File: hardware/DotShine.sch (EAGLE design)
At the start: 62 parts, among them CN1 1X4-BIG, IC1 CAT24M010TS, IC3 SI1145, J3 USB-MICROB, U1 ATMEGA328P-MU-QFN32, U2 TMP102, U3 ATSHA204-TSU, U4 JDY-16, X2 MC-RTC-RV-4162-C7-I2C, X3 S4B-ZR

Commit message: Initial bluetooth integration
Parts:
- removed X3: S4B-ZR, con-jst:S4B-ZR
- added U$4: JST-8, mihai_connectors_jst:JST-8
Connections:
- removed net N$4: LED1.CRED, R1C.2
- new net RXD_IN: LED1.CRED, R1C.2, U$4.8
- net +3V3: now also U$4.5
- net +5V: now also U$4.1; no longer X3-4.1
- net GND: now also U$4.4; no longer X3-1.1
- net OUTAB: now also U$4.2; no longer X3-3.1
- net SCL: now also U$4.6
- net SDA: now also U$4.7
- net TXD_OUT: now also U$4.3; no longer X3-2.1
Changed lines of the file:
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@@
 <?xml version="1.0" encoding="utf-8"?>
 <!DOCTYPE eagle SYSTEM "eagle.dtd">
-<eagle version="7.7.0">
+<eagle version="9.1.0">
 <drawing>
 <settings>
 <setting alwaysvectorfont="no"/>
+<setting keepoldvectorfont="yes"/>
 <setting verticaltext="up"/>
 </settings>
-<grid distance="0.1" unitdist="inch" unit="inch" style="lines" multiple="1" display="no" altdistance="0.01" altunitdist="inch" altunit="inch"/>
+<grid distance="0.05" unitdist="inch" unit="inch" style="lines" multiple="1" display="no" altdistance="0.01" altunitdist="inch" altunit="inch"/>
 <layers>
 <layer number="1" name="Top" color="4" fill="1" visible="no" active="no"/>
@@
 <layer number="59" name="tCarbon" color="7" fill="1" visible="no" active="no"/>
 <layer number="60" name="bCarbon" color="7" fill="1" visible="no" active="no"/>
+<layer number="88" name="SimResults" color="9" fill="1" visible="yes" active="yes"/>
+<layer number="89" name="SimProbes" color="9" fill="1" visible="yes" active="yes"/>
 <layer number="90" name="Modules" color="5" fill="1" visible="yes" active="yes"/>
 <layer number="91" name="Nets" color="2" fill="1" visible="yes" active="yes"/>
@@
 <part name="+3V6" library="supply1" deviceset="+3V3" device=""/>
 <part name="SUPPLY2" library="supply2" deviceset="GND" device=""/>
-<part name="SUPPLY7" library="supply2" deviceset="GND" device=""/>
-<part name="X3" library="con-jst" deviceset="?4B-ZR" device="S"/>
-<part name="P+2" library="supply1" deviceset="+5V" device=""/>
 <part name="LED2" library="SparkFun" deviceset="LED" device="0603"/>
 <part name="LED3" library="SparkFun" deviceset="LED" device="0603"/>
@@
 <part name="SUPPLY9" library="supply2" deviceset="GND" device=""/>
 <part name="+3V22" library="supply1" deviceset="+3V3" device=""/>
+<part name="U$4" library="mihai_connectors_jst" deviceset="JST-8" device=""/>
+<part name="SUPPLY12" library="supply2" deviceset="GND" device=""/>
+<part name="P+1" library="supply1" deviceset="+5V" device=""/>
+<part name="+3V23" library="supply1" deviceset="+3V3" device=""/>
 </parts>
 <sheets>
@@
 <instance part="+3V6" gate="G$1" x="43.18" y="115.57" rot="R90"/>
 <instance part="SUPPLY2" gate="GND" x="52.07" y="110.49"/>
-<instance part="SUPPLY7" gate="GND" x="97.79" y="125.73" rot="R270"/>
-<instance part="X3" gate="-1" x="111.76" y="125.73"/>
-<instance part="X3" gate="-2" x="111.76" y="123.19"/>
-<instance part="X3" gate="-3" x="111.76" y="120.65"/>
-<instance part="X3" gate="-4" x="111.76" y="118.11"/>
-<instance part="P+2" gate="1" x="83.82" y="118.11" rot="R90"/>
 <instance part="LED2" gate="G$1" x="137.16" y="142.24" rot="R90"/>
 <instance part="LED3" gate="G$1" x="139.7" y="132.08" rot="R270"/>
@@
 <instance part="SUPPLY9" gate="GND" x="137.16" y="-330.2" rot="MR270"/>
 <instance part="+3V22" gate="G$1" x="76.2" y="-317.5"/>
+<instance part="U$4" gate="G$1" x="134.62" y="-412.75"/>
+<instance part="SUPPLY12" gate="GND" x="113.03" y="-397.51" rot="R270"/>
+<instance part="P+1" gate="1" x="116.84" y="-389.89" rot="R90"/>
+<instance part="+3V23" gate="G$1" x="111.76" y="-400.05" rot="R90"/>
 </instances>
 <busses>
@@
 <pinref part="R4" gate="D" pin="2"/>
 <pinref part="SUPPLY29" gate="GND" pin="GND"/>
-</segment>
-<segment>
-<pinref part="X3" gate="-1" pin="1"/>
-<pinref part="SUPPLY7" gate="GND" pin="GND"/>
-<wire x1="106.68" y1="125.73" x2="100.33" y2="125.73" width="0.1524" layer="91"/>
 </segment>
 <segment>
@@
 <junction x="134.62" y="-330.2"/>
 </segment>
+<segment>
+<pinref part="SUPPLY12" gate="GND" pin="GND"/>
+<wire x1="129.54" y1="-397.51" x2="115.57" y2="-397.51" width="0.1524" layer="91"/>
+<pinref part="U$4" gate="G$1" pin="4"/>
+</segment>
 </net>
 <net name="SDA" class="0">
@@
 <wire x1="124.46" y1="-342.9" x2="134.62" y2="-342.9" width="0.1524" layer="91"/>
 <label x="134.62" y="-342.9" size="1.27" layer="95" xref="yes"/>
+</segment>
+<segment>
+<pinref part="U$4" gate="G$1" pin="7"/>
+<wire x1="129.54" y1="-405.13" x2="125.73" y2="-405.13" width="0.1524" layer="91"/>
+<label x="125.73" y="-405.13" size="1.27" layer="95" rot="R180" xref="yes"/>
 </segment>
 </net>
@@
 <wire x1="76.2" y1="-320.04" x2="76.2" y2="-330.2" width="0.1524" layer="91"/>
 </segment>
+<segment>
+<pinref part="U$4" gate="G$1" pin="5"/>
+<pinref part="+3V23" gate="G$1" pin="+3V3"/>
+<wire x1="129.54" y1="-400.05" x2="114.3" y2="-400.05" width="0.1524" layer="91"/>
+</segment>
 </net>
 <net name="ADCENA" class="0">
@@
 <label x="134.62" y="-340.36" size="1.27" layer="95" xref="yes"/>
 </segment>
+<segment>
+<pinref part="U$4" gate="G$1" pin="6"/>
+<wire x1="129.54" y1="-402.59" x2="125.73" y2="-402.59" width="0.1524" layer="91"/>
+<label x="125.73" y="-402.59" size="1.27" layer="95" rot="R180" xref="yes"/>
+</segment>
 </net>
 <net name="PUSH" class="0">
@@
 </segment>
 <segment>
-<pinref part="X3" gate="-2" pin="1"/>
-<wire x1="106.68" y1="123.19" x2="86.36" y2="123.19" width="0.1524" layer="91"/>
-<label x="86.36" y="123.19" size="1.27" layer="95" rot="R180" xref="yes"/>
+<wire x1="129.54" y1="-394.97" x2="110.49" y2="-394.97" width="0.1524" layer="91"/>
+<label x="110.49" y="-394.97" size="1.27" layer="95" rot="R180" xref="yes"/>
+<pinref part="U$4" gate="G$1" pin="3"/>
 </segment>
 </net>
@@
 </segment>
 </net>
-<net name="N$4" class="0">
-<segment>
-<pinref part="LED1" gate="G$1" pin="CRED"/>
-<wire x1="-27.94" y1="68.58" x2="-33.02" y2="68.58" width="0.1524" layer="91"/>
-<wire x1="-33.02" y1="68.58" x2="-33.02" y2="66.04" width="0.1524" layer="91"/>
-<pinref part="R1" gate="C" pin="2"/>
-</segment>
-</net>
 <net name="+5V" class="0">
-<segment>
-<pinref part="X3" gate="-4" pin="1"/>
-<pinref part="P+2" gate="1" pin="+5V"/>
-<wire x1="106.68" y1="118.11" x2="86.36" y2="118.11" width="0.1524" layer="91"/>
-</segment>
 <segment>
 <pinref part="P+4" gate="1" pin="+5V"/>
@@
 <pinref part="P+3" gate="1" pin="+5V"/>
 <wire x1="67.31" y1="-48.26" x2="53.34" y2="-48.26" width="0.1524" layer="91"/>
+</segment>
+<segment>
+<pinref part="P+1" gate="1" pin="+5V"/>
+<wire x1="129.54" y1="-389.89" x2="119.38" y2="-389.89" width="0.1524" layer="91"/>
+<pinref part="U$4" gate="G$1" pin="1"/>
 </segment>
 </net>
@@
 <net name="OUTAB" class="0">
 <segment>
-<pinref part="X3" gate="-3" pin="1"/>
-<wire x1="106.68" y1="120.65" x2="86.36" y2="120.65" width="0.1524" layer="91"/>
-<label x="86.36" y="120.65" size="1.27" layer="95" rot="R180" xref="yes"/>
 <pinref part="R4" gate="A" pin="2"/>
-<wire x1="106.68" y1="120.65" x2="118.11" y2="120.65" width="0.1524" layer="91"/>
-<wire x1="118.11" y1="120.65" x2="118.11" y2="132.08" width="0.1524" layer="91"/>
-<junction x="106.68" y="120.65"/>
+<wire x1="113.03" y1="132.08" x2="118.11" y2="132.08" width="0.1524" layer="91"/>
+<label x="113.03" y="132.08" size="1.27" layer="95" rot="R180" xref="yes"/>
 </segment>
 <segment>
@@
 <wire x1="76.2" y1="83.82" x2="78.74" y2="83.82" width="0.1524" layer="91"/>
 <label x="78.74" y="83.82" size="1.27" layer="95" xref="yes"/>
+</segment>
+<segment>
+<wire x1="129.54" y1="-392.43" x2="110.49" y2="-392.43" width="0.1524" layer="91"/>
+<label x="110.49" y="-392.43" size="1.27" layer="95" rot="R180" xref="yes"/>
+<pinref part="U$4" gate="G$1" pin="2"/>
 </segment>
 </net>
@@
 <pinref part="U4" gate="G$1" pin="ALED"/>
 <wire x1="124.46" y1="-347.98" x2="134.62" y2="-347.98" width="0.1524" layer="91"/>
+<label x="134.62" y="-347.98" size="1.27" layer="95" xref="yes"/>
+</segment>
+</net>
+<net name="RXD_IN" class="0">
+<segment>
+<pinref part="U$4" gate="G$1" pin="8"/>
+<wire x1="129.54" y1="-407.67" x2="125.73" y2="-407.67" width="0.1524" layer="91"/>
+<label x="125.73" y="-407.67" size="1.27" layer="95" rot="R180" xref="yes"/>
+</segment>
+<segment>
+<pinref part="LED1" gate="G$1" pin="CRED"/>
+<wire x1="-27.94" y1="68.58" x2="-33.02" y2="68.58" width="0.1524" layer="91"/>
+<wire x1="-33.02" y1="68.58" x2="-33.02" y2="66.04" width="0.1524" layer="91"/>
+<pinref part="R1" gate="C" pin="2"/>
+<wire x1="-27.94" y1="68.58" x2="-27.94" y2="38.1" width="0.1524" layer="91"/>
+<junction x="-27.94" y="68.58"/>
+<label x="-27.94" y="38.1" size="1.27" layer="95" rot="R270" xref="yes"/>
 </segment>
 </net>
@@
 which will not be processed correctly with this version.
 </note>
+<note version="8.3" severity="warning">
+Since Version 8.3, EAGLE supports URNs for individual library
+assets (packages, symbols, and devices). The URNs of those assets
+will not be understood (or retained) with this version.
+</note>
 </compatibility>

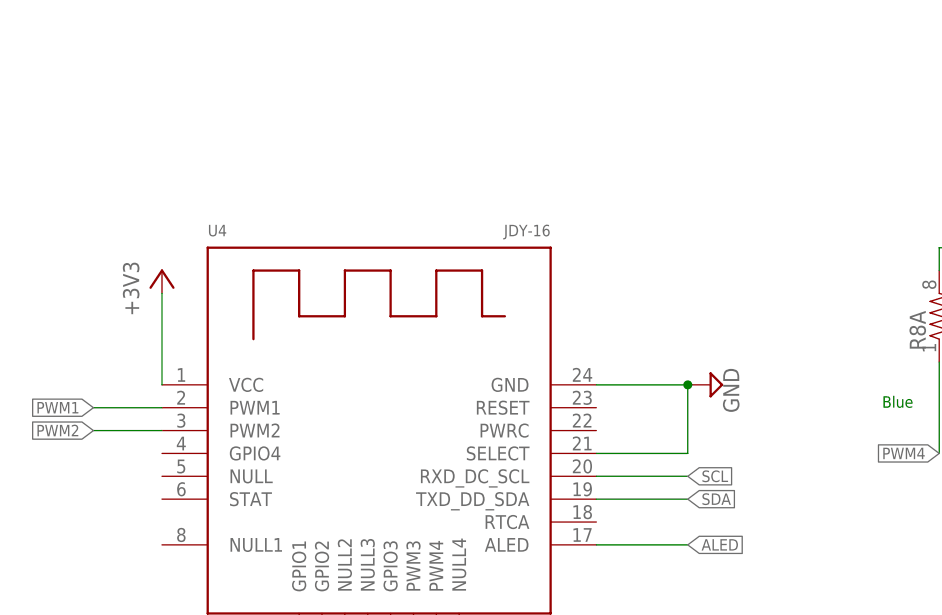
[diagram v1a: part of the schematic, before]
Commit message: Add PWRC connection for BT, needed to assert low to reenable I2C
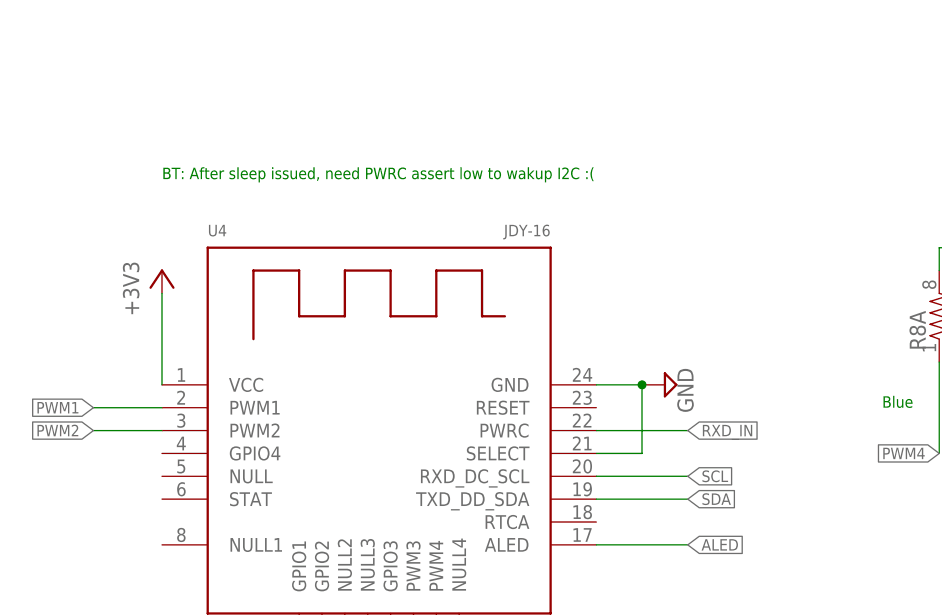
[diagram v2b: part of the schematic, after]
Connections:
- net RXD_IN: now also U4.PWRC
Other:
- note added: "BT: After sleep issued, need PWRC assert low to wakup I2C :("
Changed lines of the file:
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@@
 <setting verticaltext="up"/>
 </settings>
-<grid distance="0.05" unitdist="inch" unit="inch" style="lines" multiple="1" display="no" altdistance="0.01" altunitdist="inch" altunit="inch"/>
+<grid distance="0.1" unitdist="inch" unit="inch" style="lines" multiple="1" display="no" altdistance="0.01" altunitdist="inch" altunit="inch"/>
 <layers>
 <layer number="1" name="Top" color="4" fill="1" visible="no" active="no"/>
@@
 <text x="184.658" y="-332.74" size="1.27" layer="91">Red</text>
 <text x="156.21" y="-332.74" size="1.27" layer="91">Blue</text>
+<text x="76.2" y="-307.34" size="1.27" layer="91">BT: After sleep issued, need PWRC assert low to wakup I2C :(</text>
 </plain>
 <instances>
@@
 <instance part="R8" gate="C" x="238.76" y="-309.88" rot="R270"/>
 <instance part="R8" gate="D" x="182.88" y="-322.58" rot="R90"/>
-<instance part="SUPPLY9" gate="GND" x="137.16" y="-330.2" rot="MR270"/>
+<instance part="SUPPLY9" gate="GND" x="132.08" y="-330.2" rot="MR270"/>
 <instance part="+3V22" gate="G$1" x="76.2" y="-317.5"/>
 <instance part="U$4" gate="G$1" x="134.62" y="-412.75"/>
@@
 <pinref part="SUPPLY9" gate="GND" pin="GND"/>
 <pinref part="U4" gate="G$1" pin="GND"/>
-<wire x1="134.62" y1="-330.2" x2="124.46" y2="-330.2" width="0.1524" layer="91"/>
+<wire x1="129.54" y1="-330.2" x2="124.46" y2="-330.2" width="0.1524" layer="91"/>
 <pinref part="U4" gate="G$1" pin="SELECT"/>
-<wire x1="124.46" y1="-337.82" x2="134.62" y2="-337.82" width="0.1524" layer="91"/>
-<wire x1="134.62" y1="-337.82" x2="134.62" y2="-330.2" width="0.1524" layer="91"/>
-<junction x="134.62" y="-330.2"/>
+<wire x1="124.46" y1="-337.82" x2="129.54" y2="-337.82" width="0.1524" layer="91"/>
+<wire x1="129.54" y1="-337.82" x2="129.54" y2="-330.2" width="0.1524" layer="91"/>
+<junction x="129.54" y="-330.2"/>
 </segment>
 <segment>
@@
 <label x="-27.94" y="38.1" size="1.27" layer="95" rot="R270" xref="yes"/>
 </segment>
-</net>
+<segment>
+<pinref part="U4" gate="G$1" pin="PWRC"/>
+<wire x1="124.46" y1="-335.28" x2="134.62" y2="-335.28" width="0.1524" layer="91"/>
+<label x="134.62" y="-335.28" size="1.27" layer="95" xref="yes"/>
+</segment>
+</net>

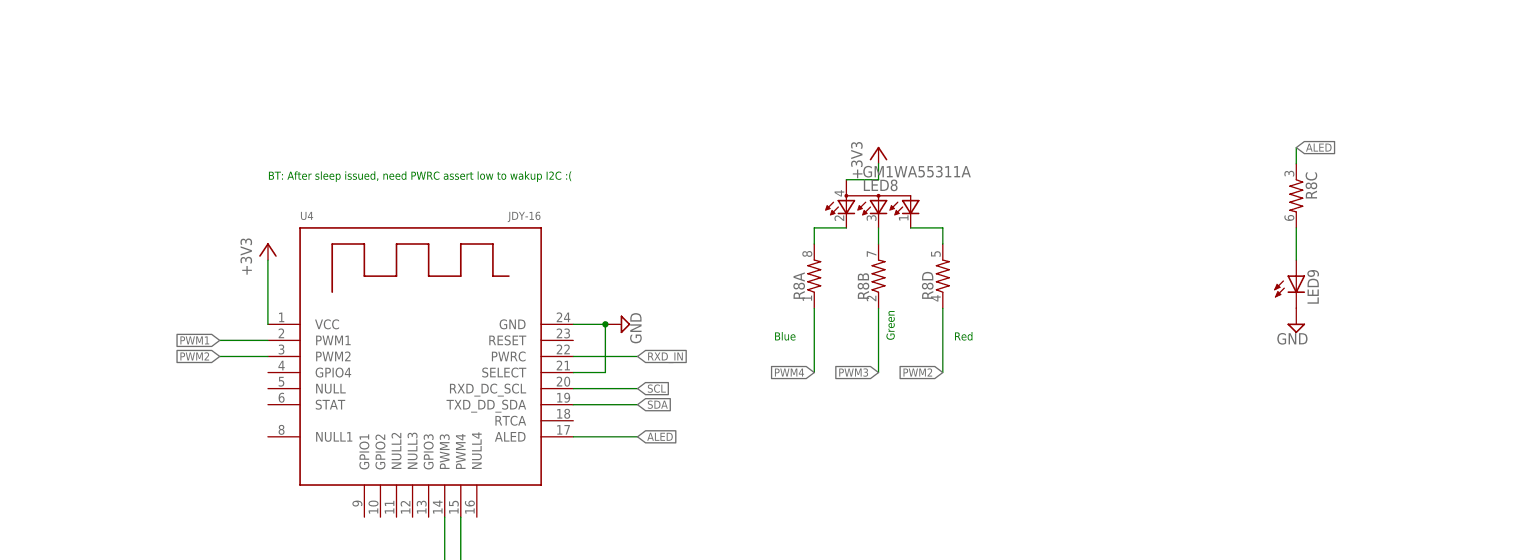
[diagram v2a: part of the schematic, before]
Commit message: Connect BT Stat to INT_MULTIPLE, SJ on ALED
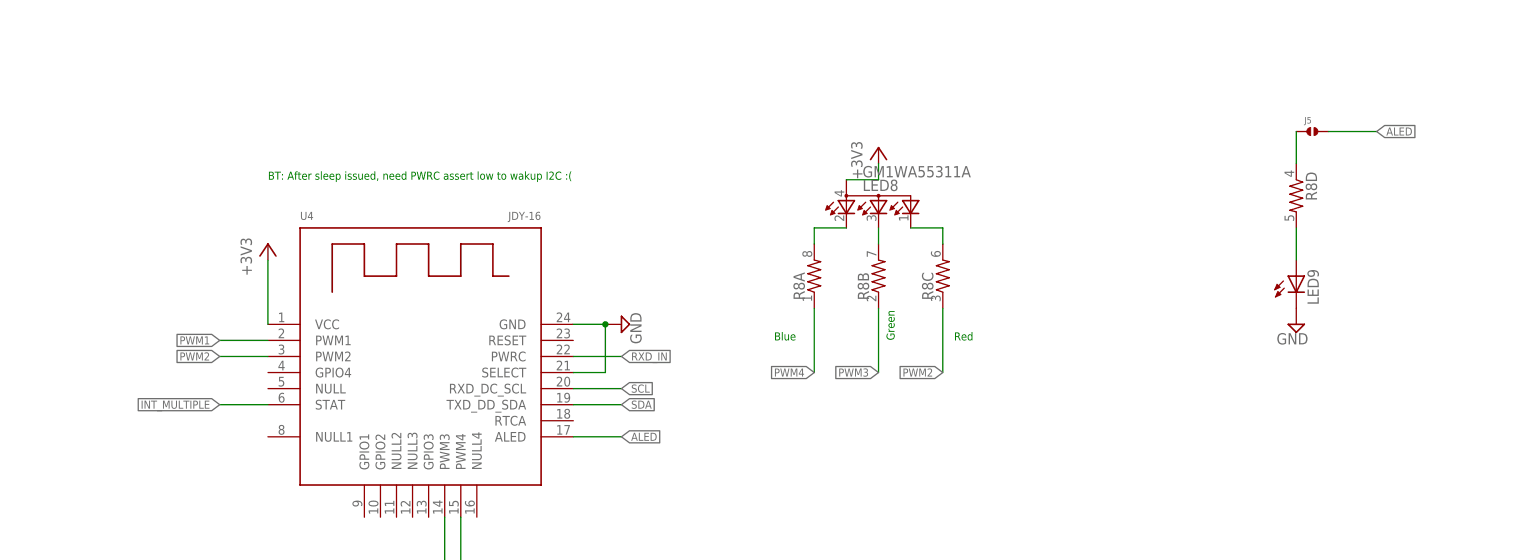
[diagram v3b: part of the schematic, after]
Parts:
- added J5: (no value), solderjumper:SOLDERJUMPER.2.MED
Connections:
- removed net BT_RED: LED8.CGREEN, R8D.2
- removed net N$34: LED9.A, R8C.2
- new net N$1: LED8.CGREEN, R8C.2
- new net N$2: J5.1, R8D.1
- new net N$4: LED9.A, R8D.2
- net ALED: now also J5.2; no longer R8C.1
- net INT_MULTIPLE: now also U4.STAT
- net PWM2: now also R8C.1; no longer R8D.1
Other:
- moved on the sheet: R8C, R8D
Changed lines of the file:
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@@
 <part name="P+1" library="supply1" deviceset="+5V" device=""/>
 <part name="+3V23" library="supply1" deviceset="+3V3" device=""/>
+<part name="J5" library="solderjumper" deviceset="SOLDERJUMPER.2" device=".MED"/>
 </parts>
 <sheets>
@@
 <instance part="R8" gate="A" x="162.56" y="-322.58" rot="R90"/>
 <instance part="R8" gate="B" x="172.72" y="-322.58" rot="R90"/>
-<instance part="R8" gate="C" x="238.76" y="-309.88" rot="R270"/>
-<instance part="R8" gate="D" x="182.88" y="-322.58" rot="R90"/>
+<instance part="R8" gate="C" x="182.88" y="-322.58" rot="R90"/>
+<instance part="R8" gate="D" x="238.76" y="-309.88" rot="R270"/>
 <instance part="SUPPLY9" gate="GND" x="132.08" y="-330.2" rot="MR270"/>
 <instance part="+3V22" gate="G$1" x="76.2" y="-317.5"/>
@@
 <instance part="P+1" gate="1" x="116.84" y="-389.89" rot="R90"/>
 <instance part="+3V23" gate="G$1" x="111.76" y="-400.05" rot="R90"/>
+<instance part="J5" gate="G$1" x="241.3" y="-299.72"/>
 </instances>
 <busses>
@@
 <segment>
 <pinref part="U4" gate="G$1" pin="TXD_DD_SDA"/>
-<wire x1="124.46" y1="-342.9" x2="134.62" y2="-342.9" width="0.1524" layer="91"/>
-<label x="134.62" y="-342.9" size="1.27" layer="95" xref="yes"/>
+<wire x1="124.46" y1="-342.9" x2="132.08" y2="-342.9" width="0.1524" layer="91"/>
+<label x="132.08" y="-342.9" size="1.27" layer="95" xref="yes"/>
 </segment>
 <segment>
@@
 <segment>
 <pinref part="U4" gate="G$1" pin="RXD_DC_SCL"/>
-<wire x1="124.46" y1="-340.36" x2="134.62" y2="-340.36" width="0.1524" layer="91"/>
-<label x="134.62" y="-340.36" size="1.27" layer="95" xref="yes"/>
+<wire x1="124.46" y1="-340.36" x2="132.08" y2="-340.36" width="0.1524" layer="91"/>
+<label x="132.08" y="-340.36" size="1.27" layer="95" xref="yes"/>
 </segment>
 <segment>
@@
 <label x="78.74" y="60.96" size="1.27" layer="95" xref="yes"/>
 </segment>
+<segment>
+<pinref part="U4" gate="G$1" pin="STAT"/>
+<wire x1="76.2" y1="-342.9" x2="68.58" y2="-342.9" width="0.1524" layer="91"/>
+<label x="68.58" y="-342.9" size="1.27" layer="95" rot="R180" xref="yes"/>
+</segment>
 </net>
 <net name="OUTAB" class="0">
@@
 </segment>
 </net>
-<net name="BT_RED" class="0">
-<segment>
-<pinref part="R8" gate="D" pin="2"/>
-<pinref part="LED8" gate="G$1" pin="CGREEN"/>
-<wire x1="182.88" y1="-317.5" x2="182.88" y2="-314.96" width="0.1524" layer="91"/>
-<wire x1="182.88" y1="-314.96" x2="177.8" y2="-314.96" width="0.1524" layer="91"/>
-</segment>
-</net>
-<net name="N$34" class="0">
-<segment>
-<pinref part="R8" gate="C" pin="2"/>
-<pinref part="LED9" gate="G$1" pin="A"/>
-<wire x1="238.76" y1="-314.96" x2="238.76" y2="-320.04" width="0.1524" layer="91"/>
-</segment>
-</net>
 <net name="BT_GREEN" class="0">
 <segment>
@@
 </segment>
 <segment>
-<pinref part="R8" gate="D" pin="1"/>
+<pinref part="R8" gate="C" pin="1"/>
 <wire x1="182.88" y1="-327.66" x2="182.88" y2="-337.82" width="0.1524" layer="91"/>
 <label x="182.88" y="-337.82" size="1.27" layer="95" rot="R180" xref="yes"/>
@@
 <net name="ALED" class="0">
 <segment>
-<pinref part="R8" gate="C" pin="1"/>
-<wire x1="238.76" y1="-304.8" x2="238.76" y2="-302.26" width="0.1524" layer="91"/>
-<label x="238.76" y="-302.26" size="1.27" layer="95" xref="yes"/>
-</segment>
-<segment>
 <pinref part="U4" gate="G$1" pin="ALED"/>
-<wire x1="124.46" y1="-347.98" x2="134.62" y2="-347.98" width="0.1524" layer="91"/>
-<label x="134.62" y="-347.98" size="1.27" layer="95" xref="yes"/>
+<wire x1="124.46" y1="-347.98" x2="132.08" y2="-347.98" width="0.1524" layer="91"/>
+<label x="132.08" y="-347.98" size="1.27" layer="95" xref="yes"/>
+</segment>
+<segment>
+<pinref part="J5" gate="G$1" pin="2"/>
+<wire x1="243.84" y1="-299.72" x2="251.46" y2="-299.72" width="0.1524" layer="91"/>
+<label x="251.46" y="-299.72" size="1.27" layer="95" xref="yes"/>
 </segment>
 </net>
@@
 <segment>
 <pinref part="U4" gate="G$1" pin="PWRC"/>
-<wire x1="124.46" y1="-335.28" x2="134.62" y2="-335.28" width="0.1524" layer="91"/>
-<label x="134.62" y="-335.28" size="1.27" layer="95" xref="yes"/>
-</segment>
-</net>
+<wire x1="124.46" y1="-335.28" x2="132.08" y2="-335.28" width="0.1524" layer="91"/>
+<label x="132.08" y="-335.28" size="1.27" layer="95" xref="yes"/>
+</segment>
+</net>
+<net name="N$4" class="0">
+<segment>
+<pinref part="R8" gate="D" pin="2"/>
+<pinref part="LED9" gate="G$1" pin="A"/>
+<wire x1="238.76" y1="-314.96" x2="238.76" y2="-320.04" width="0.1524" layer="91"/>
+</segment>
+</net>
+<net name="N$1" class="0">
+<segment>
+<pinref part="LED8" gate="G$1" pin="CGREEN"/>
+<pinref part="R8" gate="C" pin="2"/>
+<wire x1="177.8" y1="-314.96" x2="182.88" y2="-314.96" width="0.1524" layer="91"/>
+<wire x1="182.88" y1="-314.96" x2="182.88" y2="-317.5" width="0.1524" layer="91"/>
+</segment>
+</net>
+<net name="N$2" class="0">
+<segment>
+<pinref part="J5" gate="G$1" pin="1"/>
+<pinref part="R8" gate="D" pin="1"/>
+<wire x1="238.76" y1="-299.72" x2="238.76" y2="-304.8" width="0.1524" layer="91"/>
+</segment>
+</net>
